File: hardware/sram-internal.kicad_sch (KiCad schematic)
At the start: 3 parts, among them U7 IS66WV51216EBLL

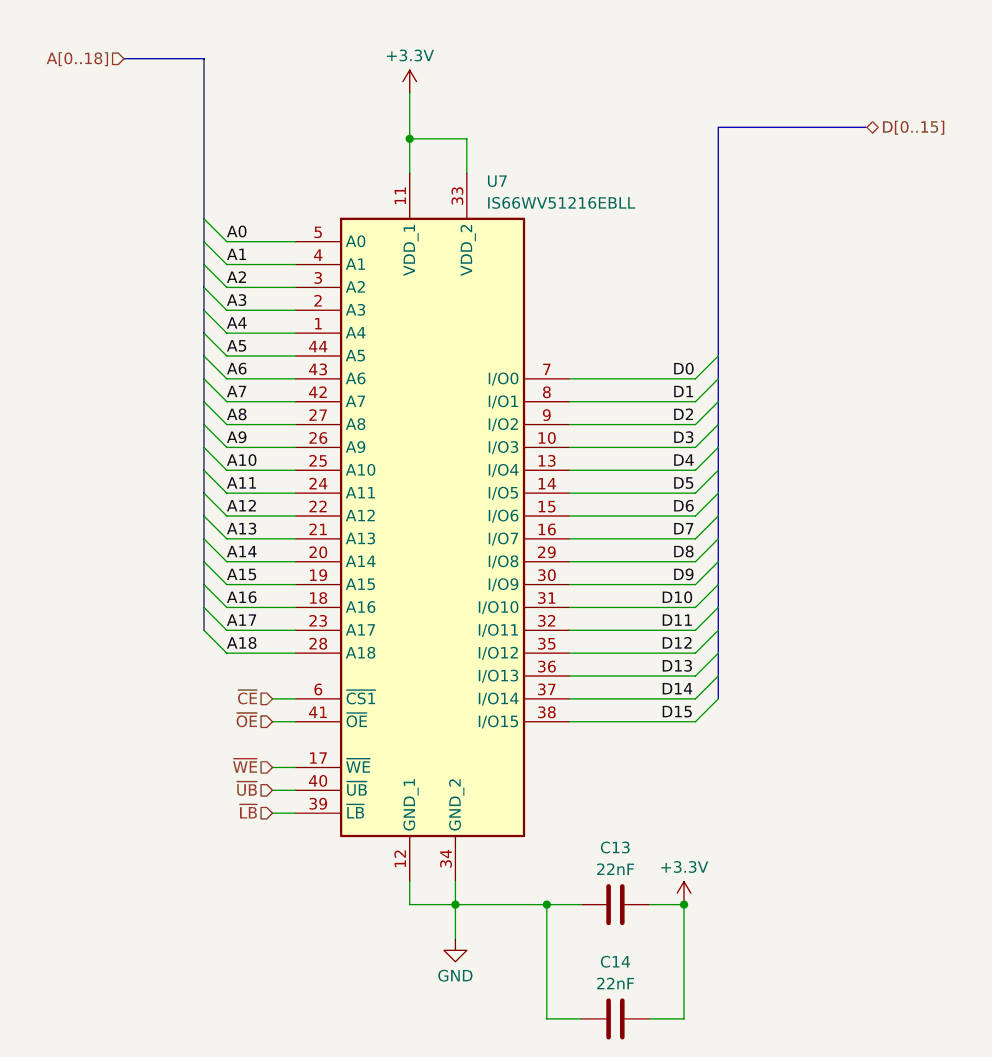
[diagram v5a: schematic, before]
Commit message: Reannotate schematics and drop debug bridges
Parts are now numbered starting at 0 for cart, 100 for SRAM, 300 for
microcontroller.

Also, drop debug bridges that made routing more difficult and had the
same names across prototype boards.

Hopefully this will help avoid naming conflicts for the unified PCB.

Also, redo prototype PCB layouts.

Now that all the names have changed, update board layouts.
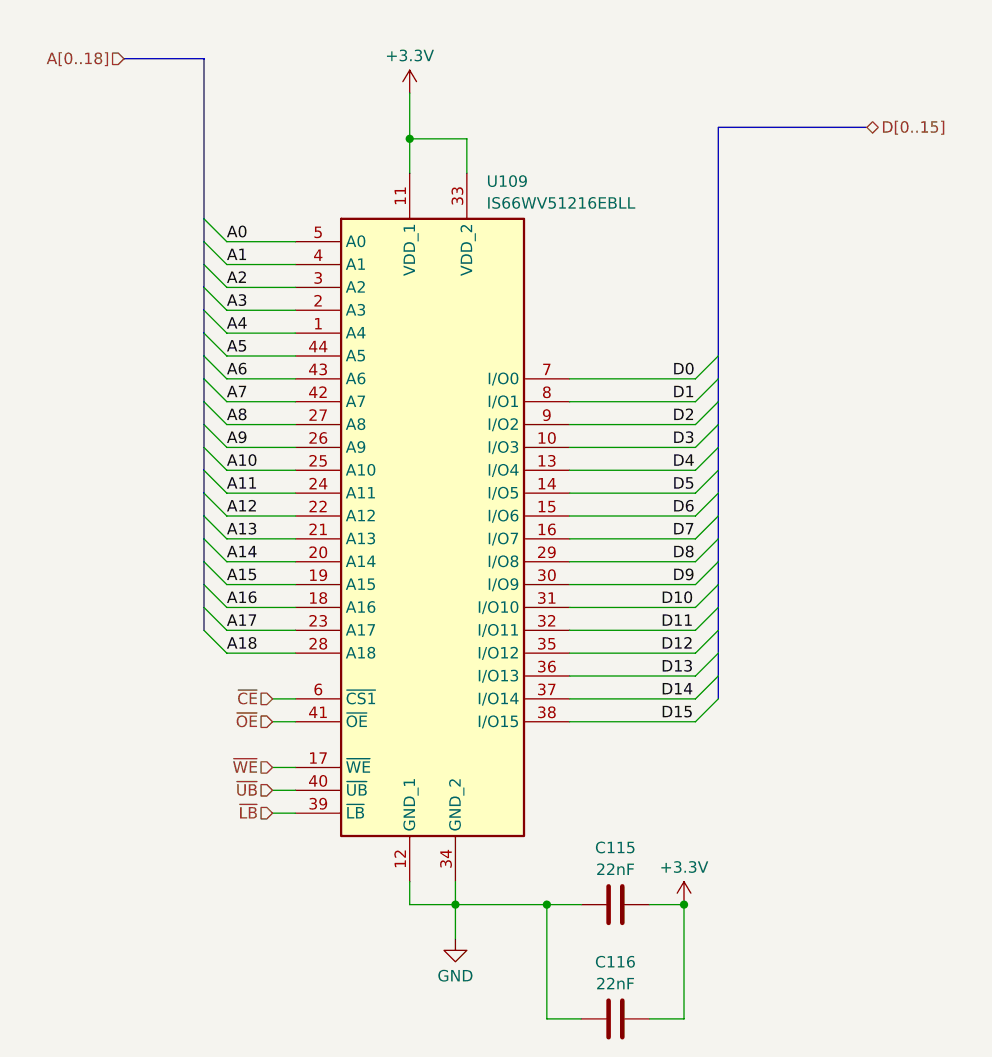
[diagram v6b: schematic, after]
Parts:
- renumbered C13 to C115, C14 to C116, U7 to U109
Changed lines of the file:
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@@
 		(dnp no)
 		(fields_autoplaced yes)
-		(property "Reference" "#PWR024"
+		(property "Reference" "#PWR0148"
 			(at 109.22 134.62 0)
 			(effects
@@
 			(project "sram-bank"
 				(path "/620c762c-1ae9-4ea9-ab1a-d023a8da85ac/de6964c0-b8e7-4813-9bb5-2e4faf4431cb/3d478650-c721-4e59-90b6-3e9b8fac63c3"
-					(reference "#PWR024")
+					(reference "#PWR0148")
+					(unit 1)
+				)
+			)
+			(project ""
+				(path "/686046a3-64dc-4761-a4ce-3e2fd65204d5/1a626848-8147-4aad-b91b-a9b45fe719ed/3d478650-c721-4e59-90b6-3e9b8fac63c3"
+					(reference "#PWR0155")
+					(unit 1)
+				)
+				(path "/686046a3-64dc-4761-a4ce-3e2fd65204d5/3e197955-3cb5-4695-aab7-f5b905115819/3d478650-c721-4e59-90b6-3e9b8fac63c3"
+					(reference "#PWR078")
 					(unit 1)
 				)
@@
 		(dnp no)
 		(fields_autoplaced yes)
-		(property "Reference" "C13"
+		(property "Reference" "C115"
 			(at 127 118.1565 90)
 			(effects
@@
 			(project "sram-bank"
 				(path "/620c762c-1ae9-4ea9-ab1a-d023a8da85ac/de6964c0-b8e7-4813-9bb5-2e4faf4431cb/3d478650-c721-4e59-90b6-3e9b8fac63c3"
-					(reference "C13")
+					(reference "C115")
+					(unit 1)
+				)
+			)
+			(project ""
+				(path "/686046a3-64dc-4761-a4ce-3e2fd65204d5/1a626848-8147-4aad-b91b-a9b45fe719ed/3d478650-c721-4e59-90b6-3e9b8fac63c3"
+					(reference "C115")
+					(unit 1)
+				)
+				(path "/686046a3-64dc-4761-a4ce-3e2fd65204d5/3e197955-3cb5-4695-aab7-f5b905115819/3d478650-c721-4e59-90b6-3e9b8fac63c3"
+					(reference "C202")
 					(unit 1)
 				)
@@
 		(dnp no)
 		(fields_autoplaced yes)
-		(property "Reference" "C14"
+		(property "Reference" "C116"
 			(at 127 130.8565 90)
 			(effects
@@
 			(project "sram-bank"
 				(path "/620c762c-1ae9-4ea9-ab1a-d023a8da85ac/de6964c0-b8e7-4813-9bb5-2e4faf4431cb/3d478650-c721-4e59-90b6-3e9b8fac63c3"
-					(reference "C14")
+					(reference "C116")
+					(unit 1)
+				)
+			)
+			(project ""
+				(path "/686046a3-64dc-4761-a4ce-3e2fd65204d5/1a626848-8147-4aad-b91b-a9b45fe719ed/3d478650-c721-4e59-90b6-3e9b8fac63c3"
+					(reference "C116")
+					(unit 1)
+				)
+				(path "/686046a3-64dc-4761-a4ce-3e2fd65204d5/3e197955-3cb5-4695-aab7-f5b905115819/3d478650-c721-4e59-90b6-3e9b8fac63c3"
+					(reference "C203")
 					(unit 1)
 				)
@@
 		(dnp no)
 		(fields_autoplaced yes)
-		(property "Reference" "#PWR025"
+		(property "Reference" "#PWR0147"
 			(at 134.62 128.27 0)
 			(effects
@@
 			(project "sram-bank"
 				(path "/620c762c-1ae9-4ea9-ab1a-d023a8da85ac/de6964c0-b8e7-4813-9bb5-2e4faf4431cb/3d478650-c721-4e59-90b6-3e9b8fac63c3"
-					(reference "#PWR025")
+					(reference "#PWR0147")
+					(unit 1)
+				)
+			)
+			(project ""
+				(path "/686046a3-64dc-4761-a4ce-3e2fd65204d5/1a626848-8147-4aad-b91b-a9b45fe719ed/3d478650-c721-4e59-90b6-3e9b8fac63c3"
+					(reference "#PWR0156")
+					(unit 1)
+				)
+				(path "/686046a3-64dc-4761-a4ce-3e2fd65204d5/3e197955-3cb5-4695-aab7-f5b905115819/3d478650-c721-4e59-90b6-3e9b8fac63c3"
+					(reference "#PWR079")
 					(unit 1)
 				)
@@
 		(dnp no)
 		(fields_autoplaced yes)
-		(property "Reference" "#PWR023"
+		(property "Reference" "#PWR0146"
 			(at 104.14 38.1 0)
 			(effects
@@
 			(project "sram-bank"
 				(path "/620c762c-1ae9-4ea9-ab1a-d023a8da85ac/de6964c0-b8e7-4813-9bb5-2e4faf4431cb/3d478650-c721-4e59-90b6-3e9b8fac63c3"
-					(reference "#PWR023")
+					(reference "#PWR0146")
+					(unit 1)
+				)
+			)
+			(project ""
+				(path "/686046a3-64dc-4761-a4ce-3e2fd65204d5/1a626848-8147-4aad-b91b-a9b45fe719ed/3d478650-c721-4e59-90b6-3e9b8fac63c3"
+					(reference "#PWR0154")
+					(unit 1)
+				)
+				(path "/686046a3-64dc-4761-a4ce-3e2fd65204d5/3e197955-3cb5-4695-aab7-f5b905115819/3d478650-c721-4e59-90b6-3e9b8fac63c3"
+					(reference "#PWR077")
 					(unit 1)
 				)
@@
 		(dnp no)
 		(fields_autoplaced yes)
-		(property "Reference" "U7"
+		(property "Reference" "U109"
 			(at 112.6841 44.1155 0)
 			(effects
@@
 			(project "sram-bank"
 				(path "/620c762c-1ae9-4ea9-ab1a-d023a8da85ac/de6964c0-b8e7-4813-9bb5-2e4faf4431cb/3d478650-c721-4e59-90b6-3e9b8fac63c3"
-					(reference "U7")
-					(unit 1)
-				)
+					(reference "U109")
+					(unit 1)
+				)
+			)
+			(project ""
+				(path "/686046a3-64dc-4761-a4ce-3e2fd65204d5/1a626848-8147-4aad-b91b-a9b45fe719ed/3d478650-c721-4e59-90b6-3e9b8fac63c3"
+					(reference "U109")
+					(unit 1)
+				)
+				(path "/686046a3-64dc-4761-a4ce-3e2fd65204d5/3e197955-3cb5-4695-aab7-f5b905115819/3d478650-c721-4e59-90b6-3e9b8fac63c3"
+					(reference "U202")
+					(unit 1)
+				)
